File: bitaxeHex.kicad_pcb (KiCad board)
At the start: 4 copper layers, 84.5 x 129.5 mm, 368 parts, among them J1 XT30, J3 Conn_02x05_Odd_Even, J4 TC2030-IDC, J5 Conn_01x04, J6 Conn_01x06, J7 USB_C_Receptacle_USB2.0, J8 Conn_01x04, J9 Conn_01x04, SW1 SWITCH-SPST, SW2 SWITCH-SPST, U1 LMR54410, U10 SGM2036-0v8, U11 SGM2036-1v8, U12 BM1366_mode1, U13 BM1366_mode1, U14 25MHz, U15 TLV3544, U16 SGM2036-1v8, U17 SGM2036-0v8, U18 BM1366_mode0, U19 25MHz, U2 RT9080-33GJ5, U20 BM1366_mode0, U21 TLV3544, U22 BM1366_mode1, U23 SGM2036-0v8, U24 SGM2036-1v8, U25 BM1366_mode1, U26 25MHz, U3 TPS546D24ARVFR, U4 MIC5504, U5 SN74AVC4T774, U6 ESP32-S3-WROOM-1, U7 TMP1075, U8 TMP1075, U9 EMC2302, Y1 32.768kHz

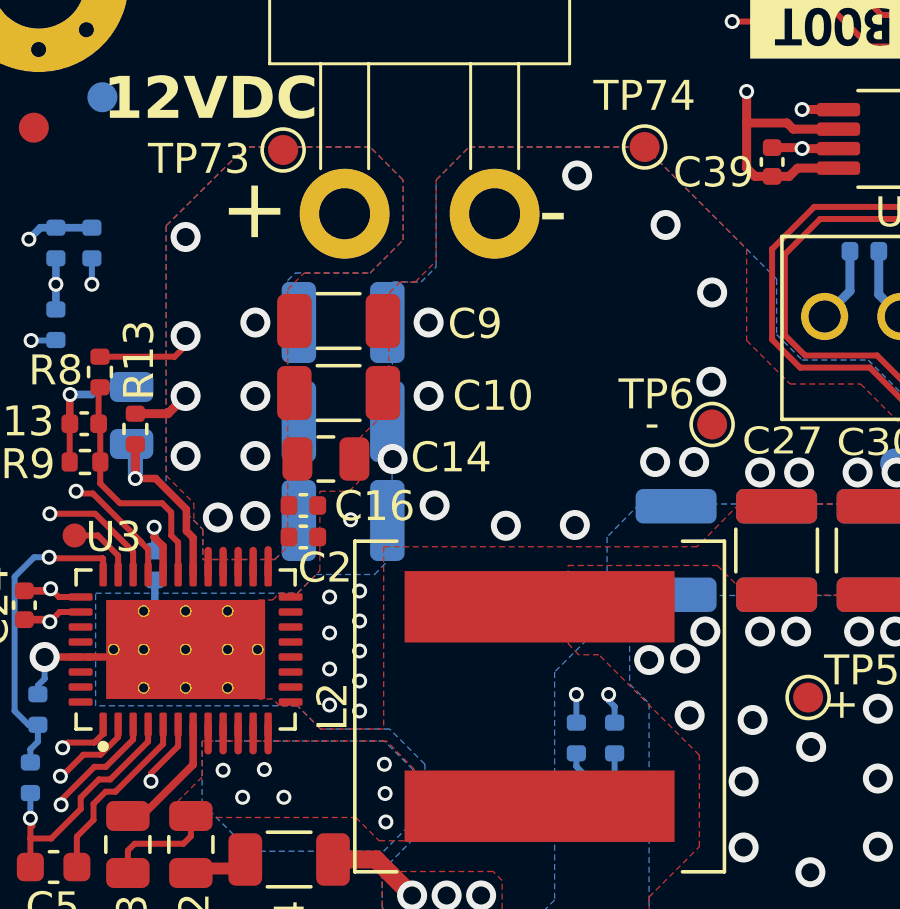
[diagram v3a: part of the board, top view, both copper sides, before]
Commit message: fix regulator input caps
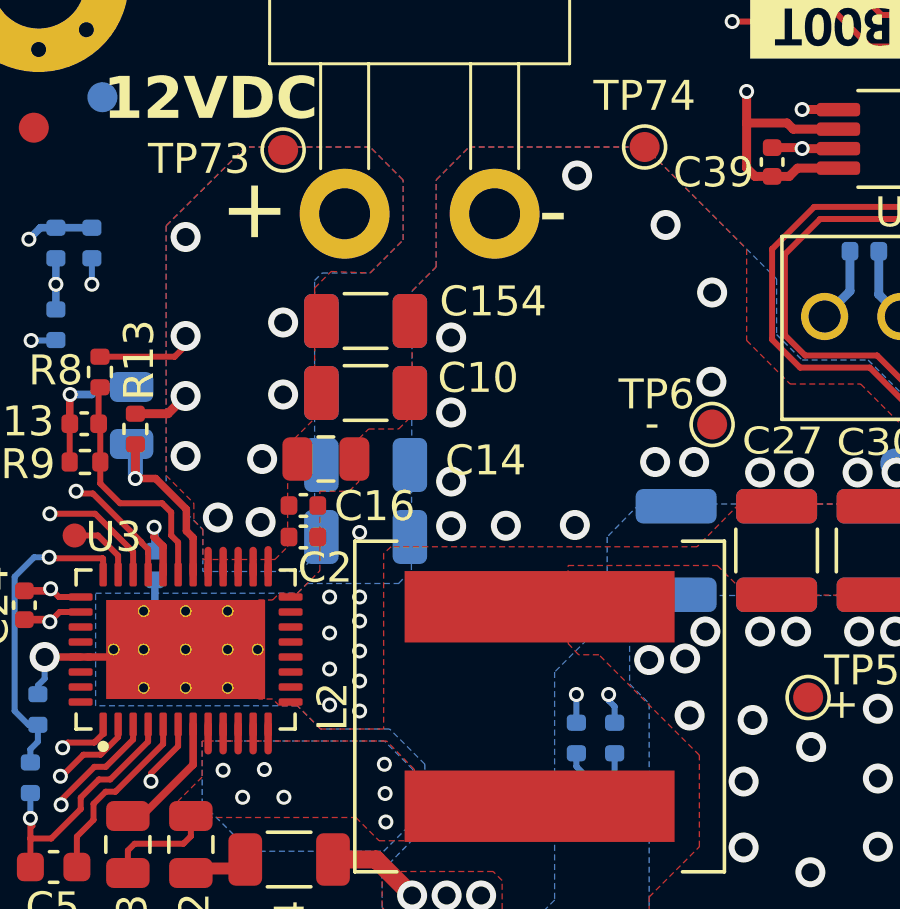
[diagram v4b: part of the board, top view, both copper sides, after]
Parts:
- added C154: 47uF, Capacitor_SMD:C_1206_3216Metric, F.Cu at (64.4, 60.8)
- C10: value 100uF -> 22uF
- C4, C7, C8: footprint Capacitor_SMD:C_1210_3225Metric -> Capacitor_SMD:C_1206_3216Metric
- C9: value 100uF -> 47uF; moved to B.Cu
- moved C8 2.47 mm to (64.4, 63.2)
- moved C7 1.63 mm to (64.4, 65.6)
- moved C4 0.93 mm to (64.4, 68.0)
- moved C10 0.90 mm to (64.4, 63.2)
- moved C9 0.90 mm to (64.4, 60.8)
